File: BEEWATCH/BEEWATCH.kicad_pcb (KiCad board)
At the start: 2 copper layers, 7 parts

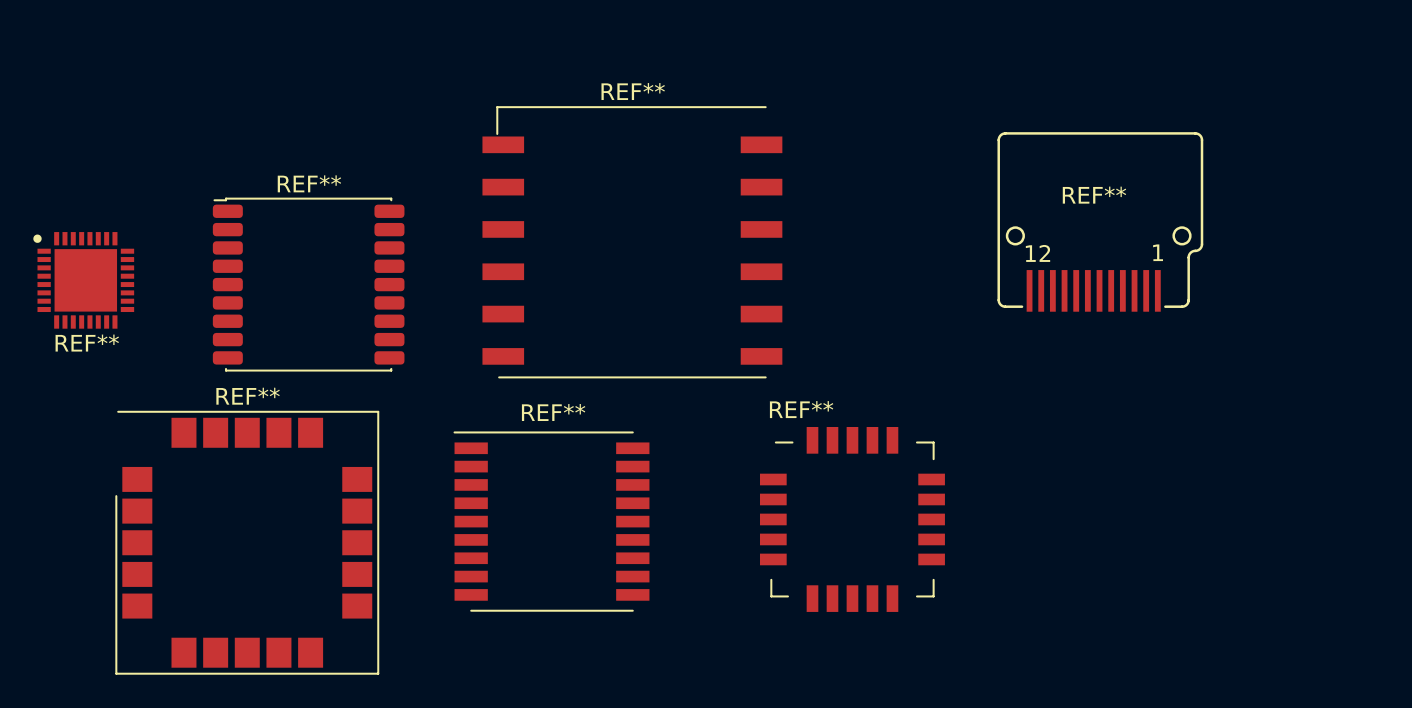
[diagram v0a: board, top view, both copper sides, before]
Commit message: Inverted F Antenna designed
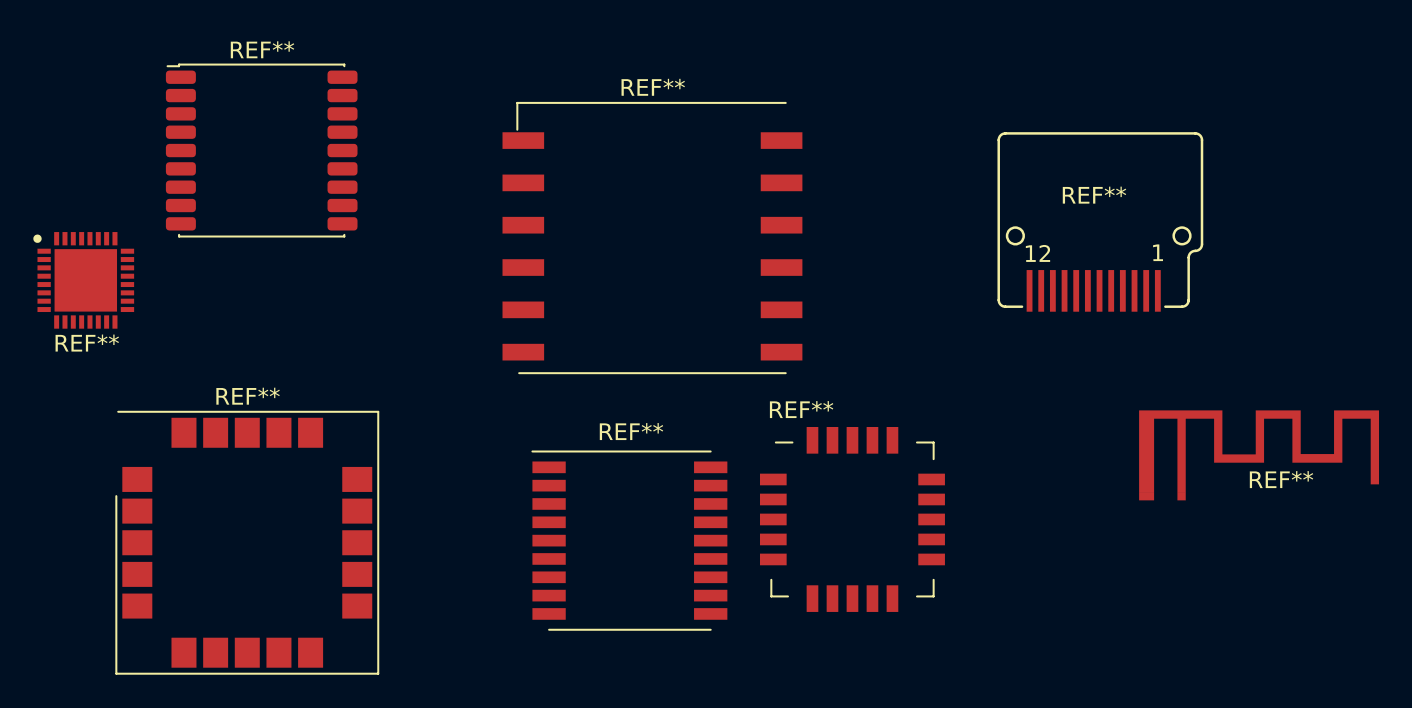
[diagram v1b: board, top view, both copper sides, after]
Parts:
- added REF**: IFA_2.4GHz, Project:IFA_2.4GHz, F.Cu at (133.9, 58.4)
- moved REF** 8.53 mm to (81.3, 37.4)
- moved REF** 4.81 mm to (103.4, 60.8)
- moved REF** 1.23 mm to (104.7, 42.7)
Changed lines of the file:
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@@
     )
+  )
+  (footprint "Project:IFA_2.4GHz" (layer "F.Cu")
+    (at 133.916 58.416)
+    (attr smd)
+    (fp_text reference "REF**" (at 8.5 -1.2 unlocked) (layer "F.SilkS")
+        (effects (font (size 1 1) (thickness 0.1)))
+    )
+    (fp_text value "IFA_2.4GHz" (at 8.5 0.3 unlocked) (layer "F.Fab")
+        (effects (font (size 1 1) (thickness 0.15)))
+    )
+    (fp_text user "${REFERENCE}" (at 8.5 1.8 unlocked) (layer "F.Fab")
+        (effects (font (size 1 1) (thickness 0.15)))
+    )
+    (fp_rect (start 0 -4.9) (end 5 -5.4)
+      (stroke (width 0) (type solid)) (fill solid) (layer "F.Cu"))
+    (fp_rect (start 0 -0.5) (end 0.9 -4.9)
+      (stroke (width 0) (type solid)) (fill solid) (layer "F.Cu"))
+    (fp_rect (start 2.3 -0.5) (end 2.8 -4.9)
+      (stroke (width 0) (type solid)) (fill solid) (layer "F.Cu"))
+    (fp_rect (start 4.5 -2.26) (end 5 -4.9)
+      (stroke (width 0) (type solid)) (fill solid) (layer "F.Cu"))
+    (fp_rect (start 5 -2.26) (end 7 -2.76)
+      (stroke (width 0) (type solid)) (fill solid) (layer "F.Cu"))
+    (fp_rect (start 7 -4.9) (end 9.7 -5.4)
+      (stroke (width 0) (type solid)) (fill solid) (layer "F.Cu"))
+    (fp_rect (start 7 -2.26) (end 7.5 -4.9)
+      (stroke (width 0) (type solid)) (fill solid) (layer "F.Cu"))
+    (fp_rect (start 9.2 -2.26) (end 9.7 -4.9)
+      (stroke (width 0) (type solid)) (fill solid) (layer "F.Cu"))
+    (fp_rect (start 9.7 -2.26) (end 11.7 -2.78)
+      (stroke (width 0) (type solid)) (fill solid) (layer "F.Cu"))
+    (fp_rect (start 11.7 -4.9) (end 14.4 -5.4)
+      (stroke (width 0) (type solid)) (fill solid) (layer "F.Cu"))
+    (fp_rect (start 11.7 -2.26) (end 12.2 -4.9)
+      (stroke (width 0) (type solid)) (fill solid) (layer "F.Cu"))
+    (fp_rect (start 13.9 -0.96) (end 14.4 -4.9)
+      (stroke (width 0) (type solid)) (fill solid) (layer "F.Cu"))
+    (pad "1" smd custom (at 0.45 -0.25) (size 0.9 0.5) (layers "F.Cu" "F.Paste" "F.Mask")
+      (zone_connect 0)
+      (options (clearance outline) (anchor rect))
+      (primitives
+        (gr_line (start 0 0) (end 0 0) (width 0.2))
+      ))
+    (pad "2" smd rect (at 2.55 -0.25) (size 0.5 0.5) (layers "F.Cu" "F.Paste" "F.Mask"))
   )
   (footprint "RF_GPS:ublox_SAM-M8Q" (layer "F.Cu")
@@
   )
   (footprint "RF_GPS:Quectel_L80-R" (layer "F.Cu")
-    (at 103.505 42.926)
+    (at 104.707767 42.671767)
     (descr "Quectel L80-R GPS Module, Patch on Top, https://www.quectel.com/UploadImage/Downlad/Quectel_L80-R_Hardware_Design_V1.2.pdf")
     (tags "quectel GPS GNSS")
@@
       (polygon
         (pts
-          (xy 104.159775 42.296)
-          (xy 104.140712 42.078111)
-          (xy 104.084103 41.866842)
-          (xy 103.991667 41.668613)
-          (xy 103.866213 41.489446)
-          (xy 103.711554 41.334787)
-          (xy 103.532388 41.209333)
-          (xy 103.334158 41.116897)
-          (xy 103.122889 41.060288)
-          (xy 102.905 41.041225)
-          (xy 102.687111 41.060288)
-          (xy 102.475842 41.116897)
-          (xy 102.277613 41.209333)
-          (xy 102.098446 41.334787)
-          (xy 101.943787 41.489446)
-          (xy 101.818333 41.668613)
-          (xy 101.725897 41.866842)
-          (xy 101.669288 42.078111)
-          (xy 101.650225 42.296)
-          (xy 101.669288 42.513889)
-          (xy 101.725897 42.725158)
-          (xy 101.818333 42.923387)
-          (xy 101.943787 43.102554)
-          (xy 102.098446 43.257213)
-          (xy 102.277612 43.382667)
-          (xy 102.475842 43.475103)
-          (xy 102.687111 43.531712)
-          (xy 102.905 43.550775)
-          (xy 103.122889 43.531712)
-          (xy 103.334158 43.475103)
-          (xy 103.532388 43.382667)
-          (xy 103.711554 43.257213)
-          (xy 103.866213 43.102554)
-          (xy 103.991667 42.923387)
-          (xy 104.084103 42.725158)
-          (xy 104.140712 42.513889)
+          (xy 105.362542 42.041767)
+          (xy 105.343479 41.823878)
+          (xy 105.28687 41.612609)
+          (xy 105.194434 41.41438)
+          (xy 105.06898 41.235213)
+          (xy 104.914321 41.080554)
+          (xy 104.735155 40.9551)
+          (xy 104.536925 40.862664)
+          (xy 104.325656 40.806055)
+          (xy 104.107767 40.786992)
+          (xy 103.889878 40.806055)
+          (xy 103.678609 40.862664)
+          (xy 103.48038 40.9551)
+          (xy 103.301213 41.080554)
+          (xy 103.146554 41.235213)
+          (xy 103.0211 41.41438)
+          (xy 102.928664 41.612609)
+          (xy 102.872055 41.823878)
+          (xy 102.852992 42.041767)
+          (xy 102.872055 42.259656)
+          (xy 102.928664 42.470925)
+          (xy 103.0211 42.669154)
+          (xy 103.146554 42.848321)
+          (xy 103.301213 43.00298)
+          (xy 103.480379 43.128434)
+          (xy 103.678609 43.22087)
+          (xy 103.889878 43.277479)
+          (xy 104.107767 43.296542)
+          (xy 104.325656 43.277479)
+          (xy 104.536925 43.22087)
+          (xy 104.735155 43.128434)
+          (xy 104.914321 43.00298)
+          (xy 105.06898 42.848321)
+          (xy 105.194434 42.669154)
+          (xy 105.28687 42.470925)
+          (xy 105.343479 42.259656)
         )
       )
@@
   )
   (footprint "RF_GPS:SIM28ML" (layer "F.Cu")
-    (at 98.679 59.69)
+    (at 103.354 60.833)
     (descr "https://simcom.ee/documents/SIM28ML/SIM28ML_Hardware%20Design_V1.01.pdf")
     (tags "SIM28ML GPS")
@@
   )
   (footprint "RF_GPS:Quectel_L70-R" (layer "F.Cu")
-    (at 84.074 45.466)
+    (at 81.256 37.42)
     (descr "Quectel L70-R, (https://www.quectel.com/product/gps-only-l70-r)")
     (tags "GPS Quectel L70-R")
@@
         (effects (font (size 1 1) (thickness 0.15)))
     )
-    (fp_text value "Quectel_L70-R" (at 0 1.5) (layer "F.Fab")
-        (effects (font (size 1 1) (thickness 0.15)))
-    )
-    (fp_text user "${REFERENCE}" (at 0 0) (layer "F.Fab")
-        (effects (font (size 1 1) (thickness 0.15)))
-    )
+    (fp_text value "Quectel_L70-R" (at 2.413 0.484) (layer "F.Fab")
+        (effects (font (size 1 1) (thickness 0.15)))
+    )
+    (fp_text user "${REFERENCE}" (at 2.413 -1.016) (layer "F.Fab")
+        (effects (font (size 1 1) (thickness 0.15)))
+    )
